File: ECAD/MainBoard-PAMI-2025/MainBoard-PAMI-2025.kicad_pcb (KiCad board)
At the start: 2 copper layers, 50 parts, among them J1 Selecteur-Robot, J10 Serial, J11 Con_Batt, J12 BAU, J13 OLED, J2 USB_B, J3 Tirette, J4 Servo, J5 Sensor_Right, J6 Sensor_Left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

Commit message: update PCB
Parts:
- added H4: MountingHole, MountingHole:MountingHole_3.2mm_M3, F.Cu at (155.0, 80.0)
- added SW1: SW_SPDT, footprints:SK-12D10 1P2T, F.Cu at (165.0, 110.0)
- moved H3 77.3 mm to (85.0, 80.0)
- moved H2 62.7 mm to (85.0, 130.0)
- moved J12 45.3 mm to (120.0, 115.0)
- moved J11 37.9 mm to (130.0, 135.0)
- moved U4 32.9 mm to (72.4, 94.0)
- moved J7 31.8 mm to (86.4, 90.2)
- moved J2 24.0 mm to (102.2, 135.1), turned to -90 degrees
- moved H1 21.0 mm to (155.0, 130.0)
- moved U3 9.21 mm to (72.4, 72.3)
- moved J8 8.03 mm to (86.4, 68.6)
- turned U1 to 180 degrees
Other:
- board outline added: 80 x 70 mm

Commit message: Everything that need to be here :)
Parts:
- removed J12: BAU, Connector_Molex:Molex_KK-396_A-41791-0002_1x02_P3.96mm_Vertical
- added R12: 330R, Resistor_SMD:R_1206_3216Metric_Pad1.30x1.75mm_HandSolder, F.Cu at (83.5, 94.8)
- added SW2: SW_Reed, Button_Switch_SMD:SW_SPST_REED_CT05-XXXX-G1, F.Cu at (106.7, 132.2)
- added SW3: SW_SPDT, PAMI-2025:UB16SKW03N-C, F.Cu at (120.0, 114.0)
- J1, J4, J7, J8: moved to B.Cu
- J11: footprint Connector_AMASS:AMASS_XT30U-F_1x02_P5.0mm_Vertical -> PAMI-2025:LP-e6 Batterie; moved to B.Cu
- J13: footprint Connector_Molex:Molex_KK-254_AE-6410-04A_1x04_P2.54mm_Vertical -> Connector_PinSocket_2.54mm:PinSocket_1x04_P2.54mm_Vertical
- J3: value Tirette -> Sensor_RIGHT; footprint Connector_Molex:Molex_KK-254_AE-6410-02A_1x02_P2.54mm_Vertical -> Connector_PinSocket_2.54mm:PinSocket_1x06_P2.54mm_Vertical; moved to B.Cu
- J5: value Sensor_Right -> Sensor_LEFT; footprint Connector_IDC:IDC-Header_2x03_P2.54mm_Vertical -> Connector_PinSocket_2.54mm:PinSocket_1x06_P2.54mm_Vertical; moved to B.Cu
- J6: value Sensor_Left -> Servo; footprint Connector_IDC:IDC-Header_2x03_P2.54mm_Vertical -> Connector_PinHeader_2.54mm:PinHeader_1x03_P2.54mm_Vertical; moved to B.Cu
- moved SW1 81.5 mm to (83.8, 103.1)
- moved U4 76.3 mm to (148.7, 94.1), turned to 90 degrees
- moved C4 70.6 mm to (84.0, 112.5), turned to 180 degrees
- moved C3 69.8 mm to (84.0, 115.0), turned to 180 degrees
- moved J4 64.7 mm to (84.4, 90.9)
- moved C5 61.9 mm to (108.6, 86.1), turned to 90 degrees
- moved R11 60.5 mm to (93.3, 82.7)
- moved R10 60.1 mm to (93.3, 80.2)
- moved J7 58.7 mm to (145.0, 93.0), turned to -90 degrees
- moved R6 56.1 mm to (88.0, 92.5), turned to 90 degrees
- moved J1 55.8 mm to (95.4, 86.6), turned to 180 degrees
- moved U3 54.9 mm to (122.8, 94.0), turned to 90 degrees
- moved J10 53.9 mm to (100.0, 89.0), turned to 180 degrees
- moved SWEn1 53.4 mm to (92.1, 117.6), turned to 180 degrees
- moved C2 52.2 mm to (124.1, 131.8), turned to -90 degrees
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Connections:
- net Servo renamed Servo01
- J1 pad 3: BotNum02 -> BotNum01
- J1 pad 4: BotNum01 -> BotNum02
- J3 pad 1: Tirette -> +3.3V
- J5 pad 5: GPIOI_RIGHT -> GPIOI_LEFT
- J5 pad 6: XSHUT_RIGHT -> XSHUT_LEFT
- J6 pad 1: +3.3V -> Net-(J6-Pin_1)
- J6 pad 2: GND -> +5VP
- J6 pad 3: SCL -> GND
- U1 pad 4: unconnected-(U1-GPIO4/TOUCH4/ADC1_CH3-Pad4) -> Servo02
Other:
- outline, holes or cut-outs redrawn

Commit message: Quick routing
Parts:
- moved C6 27.6 mm to (137.8, 84.2), turned to 45 degrees
- moved U3 26.7 mm to (149.5, 94.7)
- moved J8 26.7 mm to (145.7, 93.7)
- moved J7 24.5 mm to (120.5, 93.4)
- moved U4 24.5 mm to (124.2, 94.5)
- moved C7 23.8 mm to (112.5, 80.4), turned to 0 degrees
- moved D6 9.38 mm to (110.0, 122.0)
- moved D7 8.48 mm to (109.3, 117.5)
- moved C9 6.51 mm to (90.0, 115.6), turned to 180 degrees
- moved SWEn1 5.82 mm to (97.9, 118.1)
- moved C2 0.06 mm to (124.0, 131.8)
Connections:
- C10 pad 2: +5VP -> +3.3V
- D1 pad 1: +5VP -> +3.3V
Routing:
- net +3.3V: track 0.00 -> 179.3 mm, vias 0 -> 2
- net +5VP: track 0.00 -> 151.1 mm
- net SDA: track 0.00 -> 99.2 mm, vias 0 -> 2
- net SCL: track 0.00 -> 99.1 mm, vias 0 -> 2
- net XSHUT_RIGHT: track 0.00 -> 62.6 mm, vias 0 -> 2
- net RightDir: track 0.00 -> 52.6 mm
- net LeftMS2: track 0.00 -> 50.7 mm
- net RightStep: track 0.00 -> 48.2 mm
- net LED_Status: track 0.00 -> 39.2 mm, vias 0 -> 2
- net Net-(J2-VBUS): track 0.00 -> 38.1 mm
- net EnDriver: track 0.00 -> 37.3 mm
- net LeftMS1: track 0.00 -> 37.2 mm, vias 0 -> 1
- net /D+: track 0.00 -> 32.5 mm
- net +BATT: track 0.00 -> 30.7 mm, vias 0 -> 1
- net LeftDir: track 0.00 -> 28.4 mm
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- added copper zone on B.Cu, net GND
- added copper zone on F.Cu, net GND

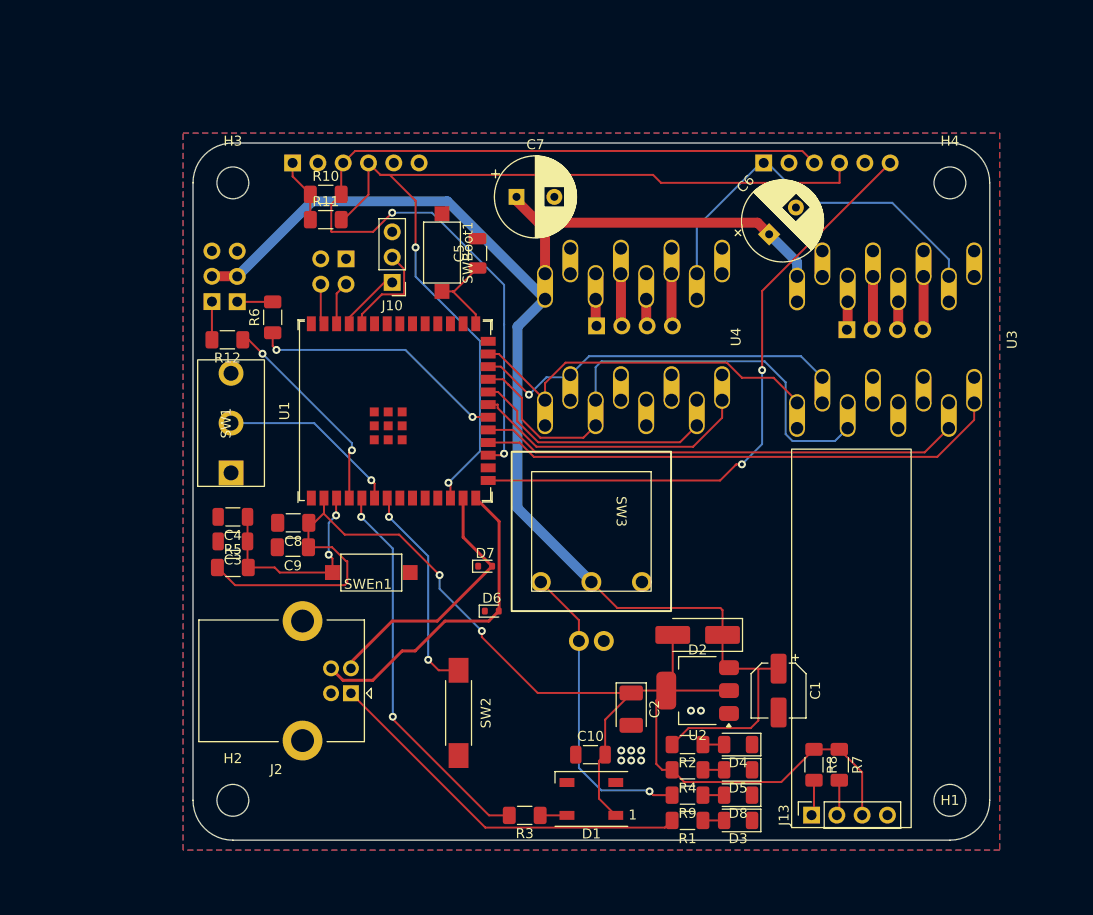
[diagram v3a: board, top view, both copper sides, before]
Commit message: Optimize routing
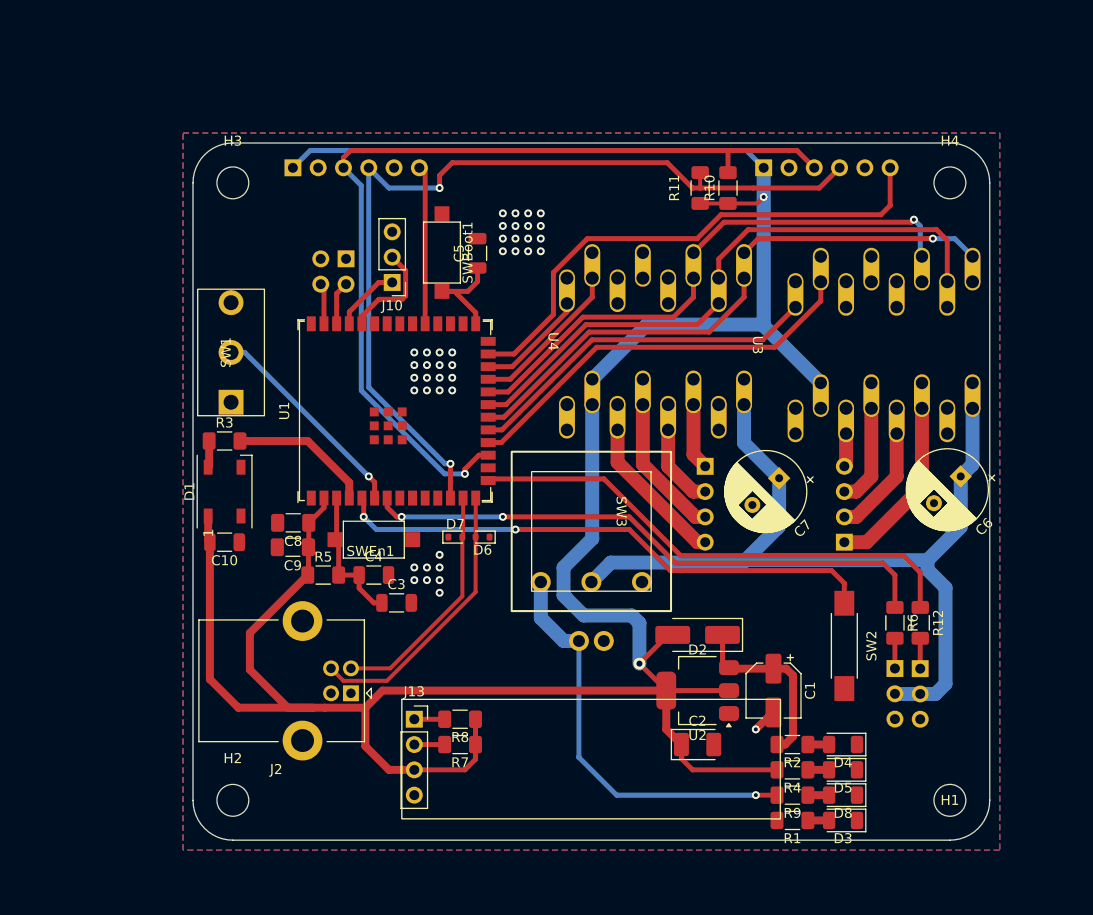
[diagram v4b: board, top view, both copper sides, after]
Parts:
- moved J6 80.1 mm to (153.0, 127.8), turned to 180 degrees
- moved J4 75.6 mm to (150.5, 127.8), turned to 180 degrees
- moved R12 75.2 mm to (153.0, 123.2), turned to -90 degrees
- moved R6 69.6 mm to (150.5, 123.2), turned to -90 degrees
- moved R3 48.2 mm to (83.2, 104.9), turned to 0 degrees
- moved D1 48.1 mm to (83.2, 110.0), turned to 90 degrees
- moved C10 42.5 mm to (83.2, 115.1), turned to 180 degrees
- moved J13 41.0 mm to (102.2, 132.9), turned to 0 degrees
- moved R10 40.4 mm to (133.7, 79.5), turned to 90 degrees
- moved SW2 39.3 mm to (145.4, 125.5)
- moved C7 38.6 mm to (138.9, 108.7), turned to -135 degrees
- moved R7 38.1 mm to (106.8, 135.4), turned to 180 degrees
- moved R11 37.7 mm to (130.9, 79.5), turned to 90 degrees
- moved R8 35.8 mm to (106.8, 132.9), turned to 180 degrees
- moved C6 31.0 mm to (157.1, 108.5), turned to -135 degrees
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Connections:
- U1 pad 15: XSHUT_RIGHT -> Servo02
- U1 pad 18: RightDir -> RightStep
- U1 pad 19: RightStep -> RightDir
- U1 pad 20: Servo01 -> EnDriver
- U1 pad 21: LeftDir -> LeftMS1
- U1 pad 22: LeftStep -> LeftMS2
- U1 pad 23: LeftMS2 -> LeftStep
- U1 pad 24: LeftMS1 -> LeftDir
- U1 pad 25: EnDriver -> XSHUT_RIGHT
- U1 pad 4: Servo02 -> LED_Status
- U1 pad 5: LED_Status -> Tirette
- U1 pad 7: Tirette -> Servo01
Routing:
- net +3.3V: track 179.3 -> 277.5 mm
- net +5VP: track 151.1 -> 107.7 mm
- net Net-(J2-VBUS): track 38.1 -> 0.00 mm
- net Tirette: track 21.4 -> 55.0 mm
- net Servo01: track 25.9 -> 58.0 mm
- net Servo02: track 20.9 -> 50.8 mm, vias 2 -> 0
- net LED_Status: track 39.2 -> 14.3 mm, vias 2 -> 0
- net LeftMS1: track 37.2 -> 58.0 mm, vias 1 -> 0
- net EnDriver: track 37.3 -> 56.9 mm, vias 0 -> 1
- net LeftDir: track 28.4 -> 11.0 mm
- net RightDir: track 52.6 -> 36.0 mm
- net XSHUT_LEFT: track 0.00 -> 16.4 mm
- net Net-(J8-Pin_1): track 2.84 -> 18.0 mm
- net Net-(J7-Pin_3): track 2.74 -> 14.5 mm
- net +BATT: track 30.7 -> 41.6 mm
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
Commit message: Update PCB
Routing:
- net Net-(J2-VBUS): track 0.00 -> 54.3 mm, vias 0 -> 1
- net SCL: track 95.2 -> 131.4 mm, vias 1 -> 2
- net SDA: track 93.3 -> 119.8 mm, vias 2 -> 3
- net +5VP: track 107.7 -> 123.8 mm
- net +3.3V: track 277.5 -> 272.4 mm, vias 2 -> 4
- net GND: vias 41 -> 42
- added copper zone on F.Cu, net +3.3V

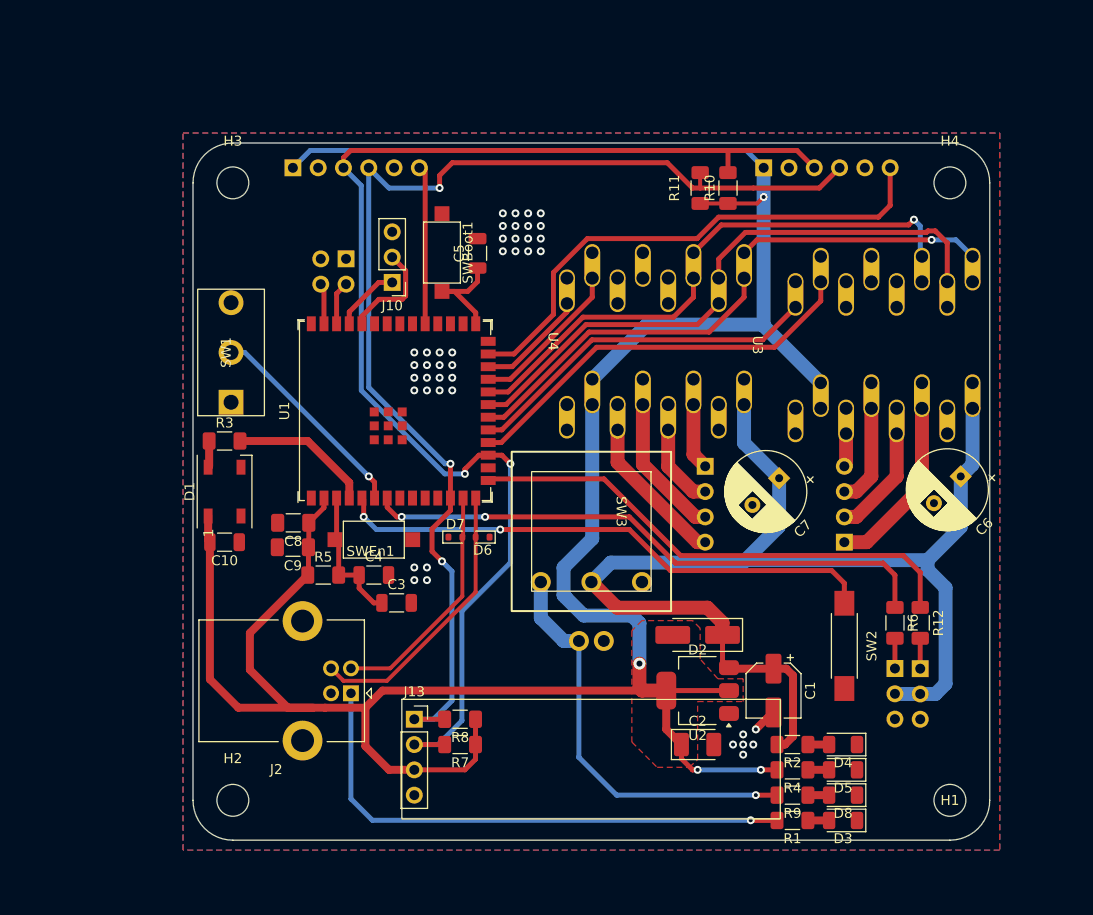
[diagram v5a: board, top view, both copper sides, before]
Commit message: Change switch + regulator + Servo Power
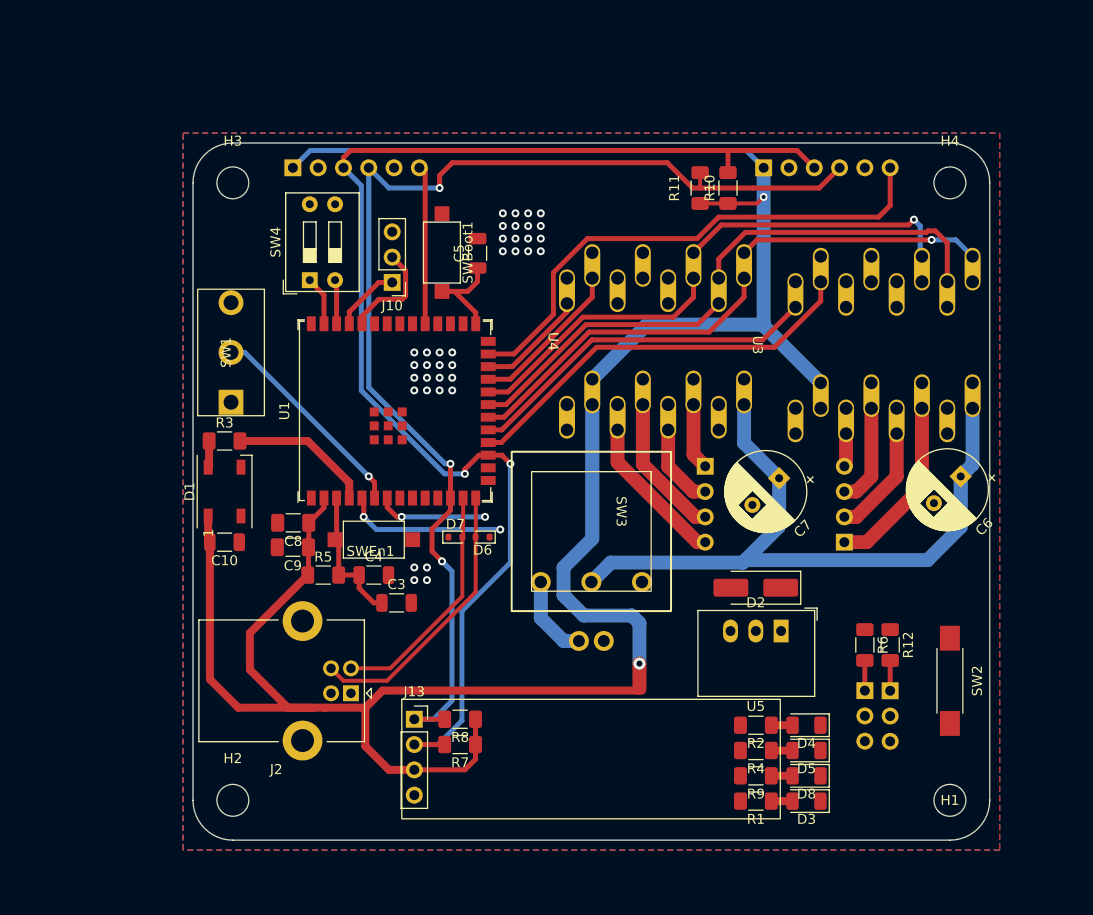
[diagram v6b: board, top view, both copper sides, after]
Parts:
- removed C1: 10uF, Capacitor_SMD:CP_Elec_5x5.4
- removed C2: 22uF, Capacitor_Tantalum_SMD:CP_EIA-3528-12_Kemet-T_Pad1.50x2.35mm_HandSolder
- removed J1: Selecteur-Robot, Connector_PinHeader_2.54mm:PinHeader_2x02_P2.54mm_Vertical
- removed U2: AMS1117-3.3, Package_TO_SOT_SMD:SOT-223-3_TabPin2
- added SW4: SW_DIP_x02, Button_Switch_THT:SW_DIP_SPSTx02_Slide_9.78x7.26mm_W7.62mm_P2.54mm, F.Cu at (91.7, 88.8)
- added U5: R-78E3.3-1.0, Converter_DCDC:Converter_DCDC_RECOM_R-78E-0.5_THT, F.Cu at (139.1, 124.0)
- moved SW2 11.2 mm to (156.0, 129.0)
- moved D2 7.52 mm to (136.5, 119.7)
- moved D8 4.15 mm to (141.6, 138.5)
- moved D3 4.15 mm to (141.6, 141.1)
- moved D4 4.15 mm to (141.6, 133.5)
- moved D5 4.15 mm to (141.6, 136.0)
- moved R9 4.15 mm to (136.5, 138.5)
- moved R1 4.15 mm to (136.5, 141.1)
- moved R2 4.15 mm to (136.5, 133.5)
- moved R4 4.15 mm to (136.5, 136.0)
- moved J6 3.75 mm to (150.0, 130.0)
- moved R12 3.75 mm to (150.0, 125.4)
- moved J4 3.75 mm to (147.5, 130.0)
- moved R6 3.75 mm to (147.5, 125.4)
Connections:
- J4 pad 2: +5VP -> +3.3V
- J6 pad 2: +5VP -> +3.3V
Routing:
- net Net-(J2-VBUS): track 54.3 -> 0.00 mm, vias 1 -> 0
- net +5VP: track 123.8 -> 70.6 mm
- net Servo02: track 50.8 -> 0.00 mm
- net Servo01: track 58.0 -> 11.2 mm
- net Tirette: track 55.0 -> 16.2 mm
- net +BATT: track 41.6 -> 8.40 mm, vias 1 -> 0
- net +3.3V: track 272.4 -> 245.4 mm, vias 4 -> 2
- net GND: track 2.48 -> 0.00 mm, vias 42 -> 36
- net BotNum02: track 4.11 -> 4.97 mm
- removed copper zone on F.Cu, net +3.3V

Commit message: add sensor center
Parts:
- added J1: Sensor_Center, Connector_PinSocket_2.54mm:PinSocket_1x06_P2.54mm_Vertical, B.Cu at (113.5, 77.5)

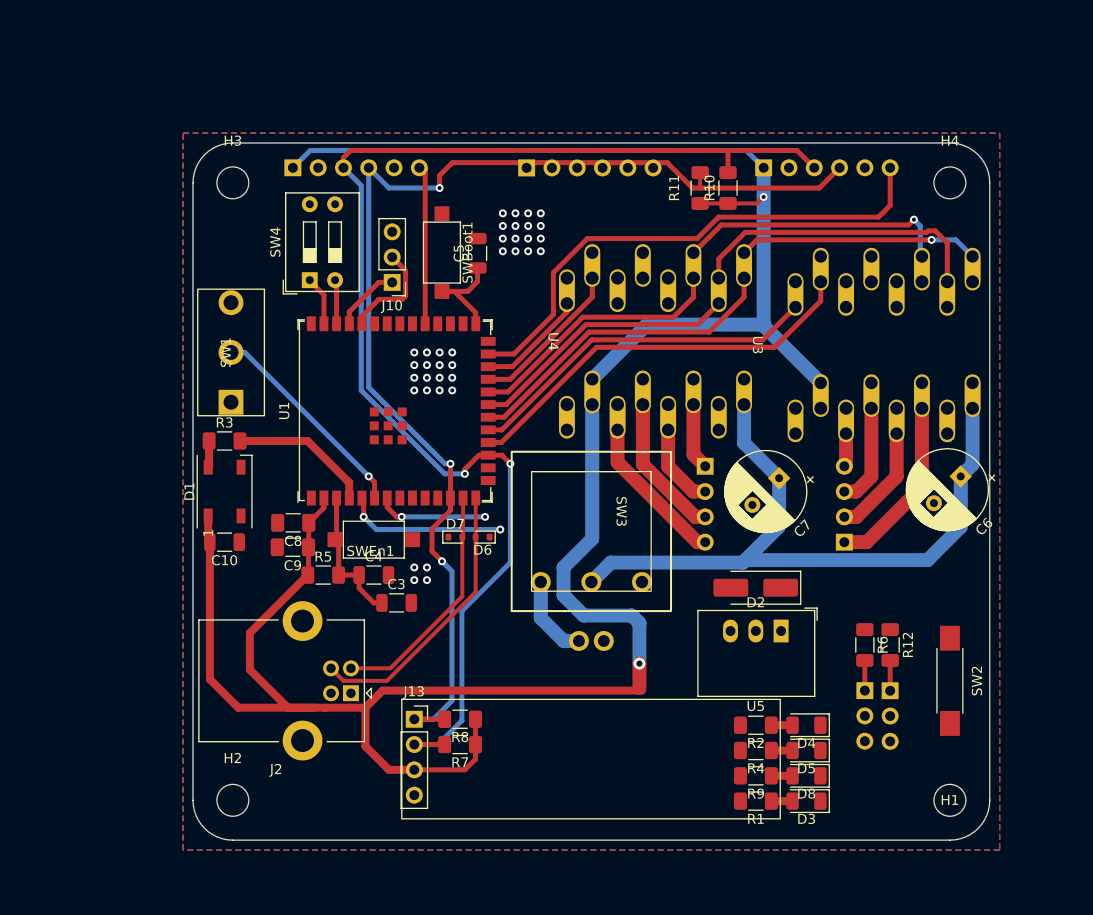
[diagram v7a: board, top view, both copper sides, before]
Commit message: new sensor position - new PCB size
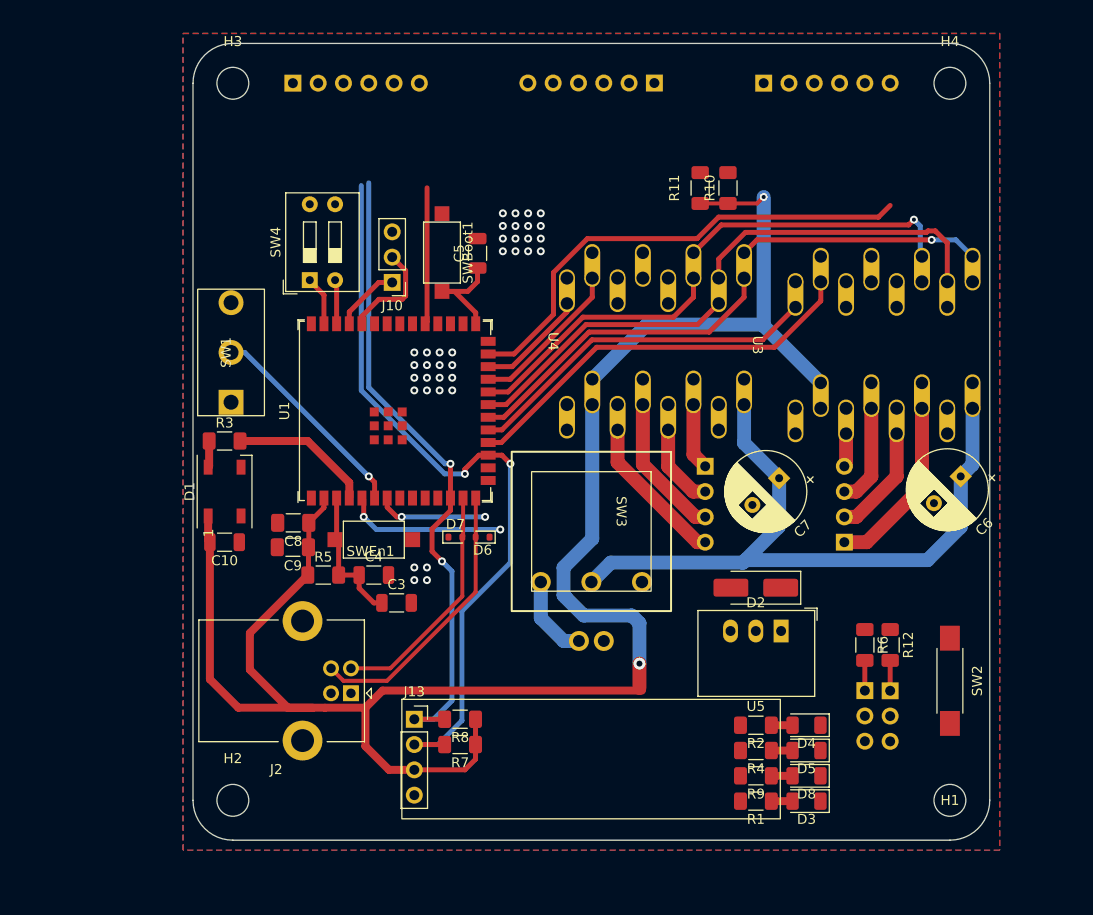
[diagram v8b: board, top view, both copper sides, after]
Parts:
- moved J1 15.4 mm to (126.3, 69.0), turned to 90 degrees
- moved H3 10.0 mm to (84.0, 69.0)
- moved H4 10.0 mm to (156.0, 69.0)
- moved J3 8.50 mm to (137.3, 69.0)
- moved J5 8.50 mm to (90.0, 69.0)
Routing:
- net SDA: track 119.8 -> 64.9 mm, vias 3 -> 2
- net SCL: track 131.4 -> 77.1 mm
- net +3.3V: track 245.4 -> 193.7 mm
- net XSHUT_RIGHT: track 53.3 -> 49.0 mm
- net XSHUT_LEFT: track 16.4 -> 13.7 mm
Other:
- board size 80 x 70 mm -> 80 x 80 mm
